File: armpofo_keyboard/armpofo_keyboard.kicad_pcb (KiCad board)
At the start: 2 copper layers, 180 x 76 mm, 94 parts, among them J1 Conn_01x16, M1 2,5mm, M10 2,5mm, M11 2,5mm, M12 2,5mm, M13 2,5mm, M14 2,5mm, M15 2,5mm, M16 2,5mm, M17 2,5mm, M18 2,5mm, M2 2,5mm, M3 2,5mm, M4 2,5mm, M5 2,5mm, M6 2,5mm, M7 2,5mm, M8 2,5mm, M9 2,5mm, SW1 Backspace, SW10 4, SW11 3, SW12 2, SW13 1, SW14 ESC, SW15 ], SW16 [, SW17 P, SW18 O, SW19 I, SW2 =+, SW20 U, SW21 Y, SW22 T, SW23 R, SW24 E, SW25 W, SW26 Q, SW27 TAB, SW28 ENTER, SW29 CAPS, SW3 -_, SW30 ' ", SW31 ;:, SW32 L, SW33 K, SW34 J, SW35 H, SW36 G, SW37 F, SW38 D, SW39 S, SW4 0, SW40 A, SW41 RSH, SW42 INS DEL, SW43 /?, SW44 .>, SW45 ,<, SW46 M, SW47 N, SW48 B, SW49 V, SW5 9, SW50 C, SW51 X, SW52 Z, SW53 \|, SW54 LSH, SW55 RIGHT, SW56 DOWN, SW57 UP, SW58 LEFT, SW59 SPACE, SW6 8, SW60 SPACE, SW61 ALT, SW62 CTRL, SW63 ATARI, SW64 FN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

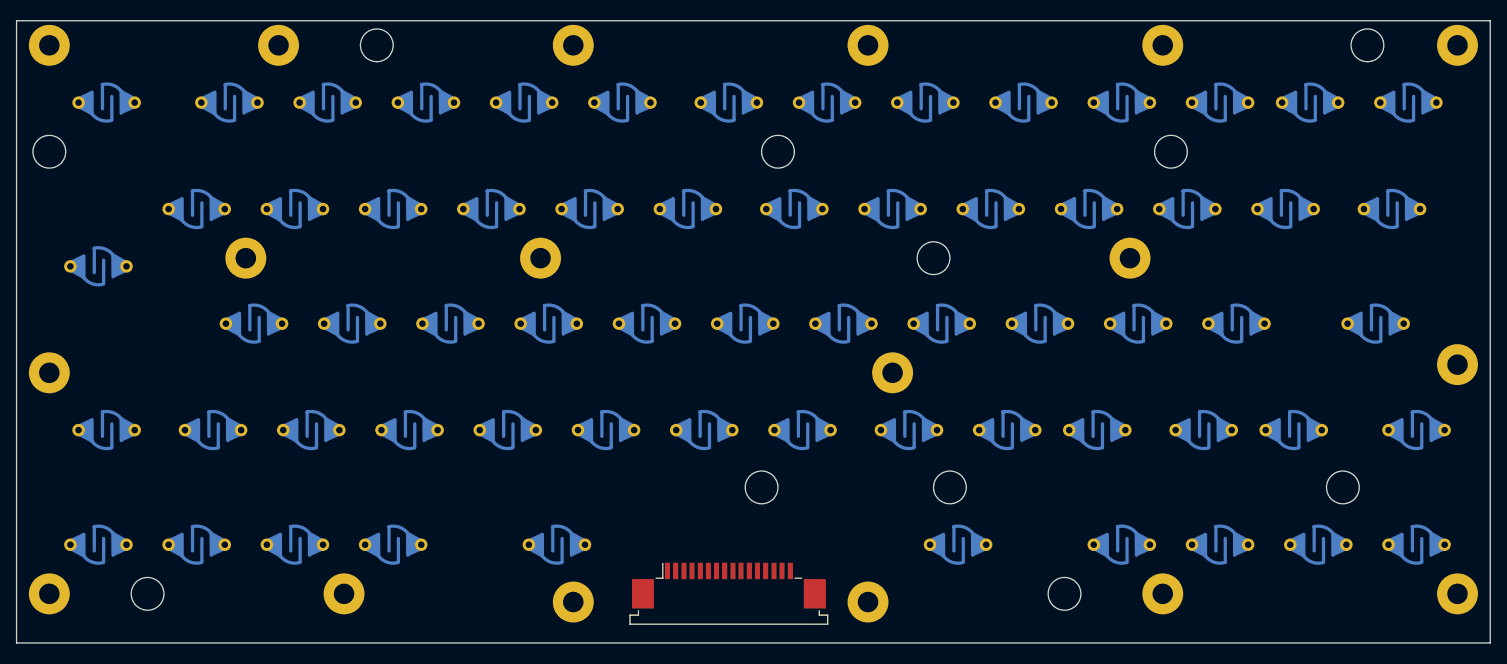
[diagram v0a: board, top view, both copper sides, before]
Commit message: holes are arranged to their final place
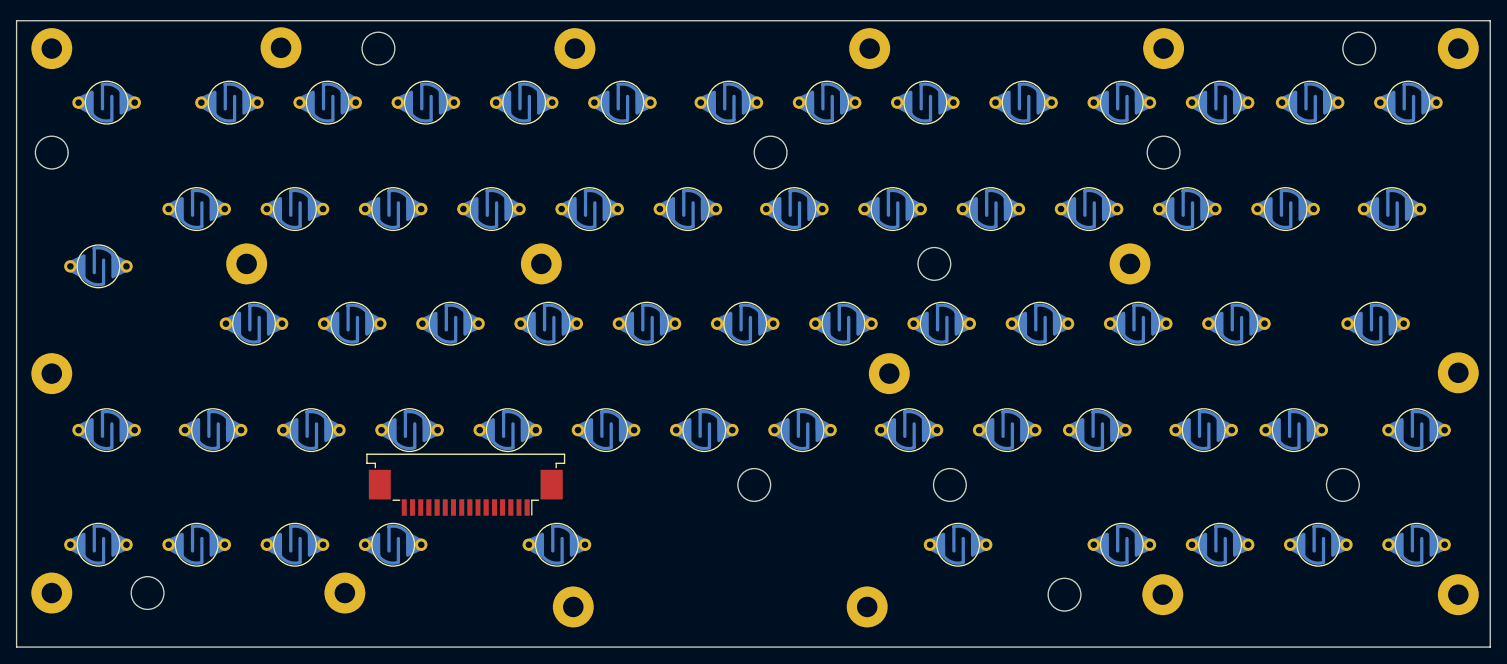
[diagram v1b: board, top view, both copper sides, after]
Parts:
- moved J1 34.1 mm to (54.9, -52.3), turned to 180 degrees
- moved H2 1.08 mm to (164.0, -106.6)
- moved M12 1.00 mm to (176.1, -67.0)
- moved H7 0.95 mm to (90.1, -53.3)
- moved H4 0.91 mm to (92.1, -93.9)
- moved H5 0.91 mm to (140.1, -93.9)
- moved M7 0.71 mm to (28.1, -80.3)
- moved H6 0.71 mm to (112.1, -80.3)
- moved M8 0.71 mm to (64.1, -80.3)
- moved M9 0.70 mm to (136.0, -80.3)
- moved M18 0.61 mm to (103.9, -38.4)
- moved M17 0.60 mm to (68.0, -38.4)
- moved M6 0.50 mm to (4.30, -106.6)
- moved H1 0.45 mm to (44.2, -106.6)
- moved M2 0.45 mm to (68.2, -106.6)
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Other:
- board size 180 x 76 mm -> 180 x 76.5 mm

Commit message: key landing at the final positions
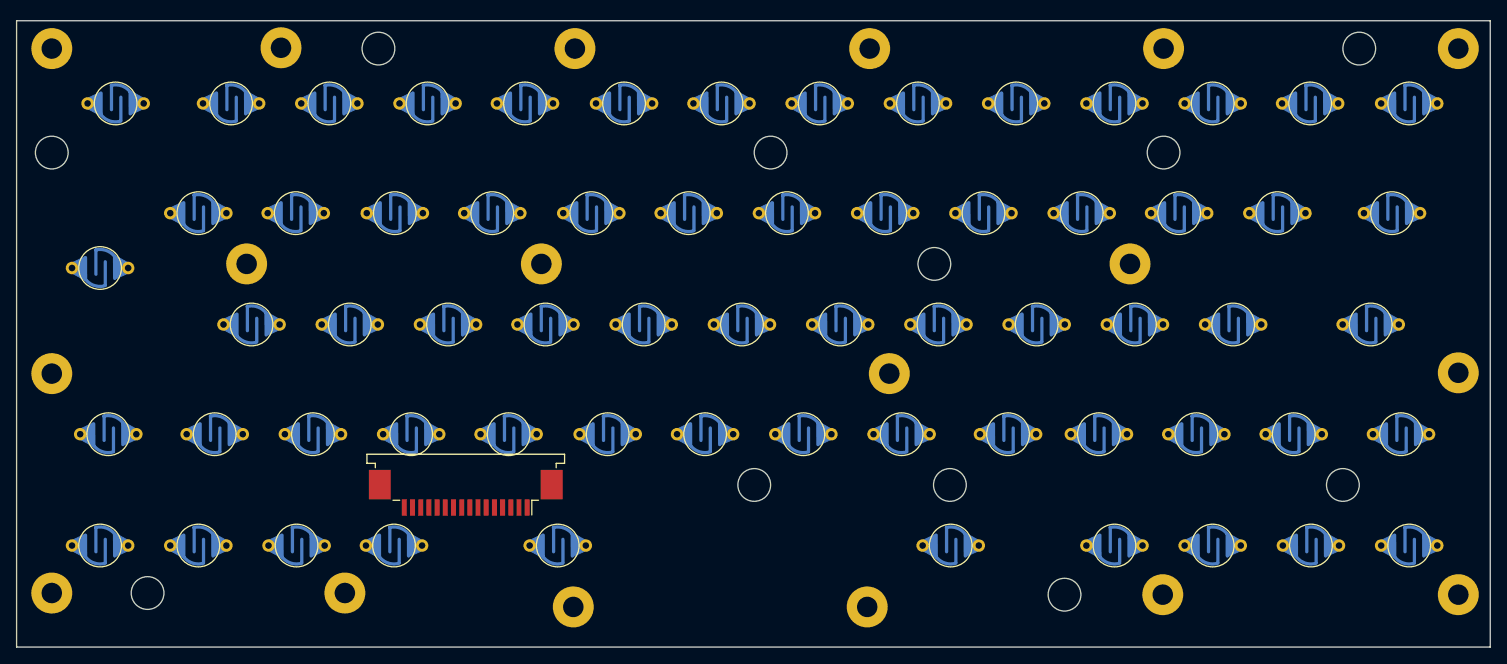
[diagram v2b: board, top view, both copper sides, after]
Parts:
- moved SW54 1.96 mm to (169.1, -59.5)
- moved SW25 1.12 mm to (142.0, -86.5)
- moved SW26 1.12 mm to (154.0, -86.5)
- moved SW1 1.10 mm to (12.1, -99.9)
- moved SW21 1.03 mm to (94.1, -86.5)
- moved SW22 1.03 mm to (106.1, -86.5)
- moved SW23 1.03 mm to (118.1, -86.5)
- moved SW24 1.03 mm to (130.1, -86.5)
- moved SW49 1.03 mm to (108.1, -59.5)
- moved SW52 1.03 mm to (144.1, -59.5)
- moved SW60 0.91 mm to (114.1, -45.9)
- moved SW61 0.91 mm to (134.1, -45.9)
- moved SW62 0.91 mm to (146.1, -45.9)
- moved SW63 0.91 mm to (158.1, -45.9)
- moved SW64 0.91 mm to (170.1, -45.9)
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
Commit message: small align adjustments
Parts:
- moved SW50 1.00 mm to (120.1, -59.5)
- moved H11 0.20 mm to (128.0, -39.7)
- moved H3 0.14 mm to (4.20, -93.8)
- moved H10 0.14 mm to (16.1, -40.0)
- moved M16 0.14 mm to (40.0, -40.0)
- moved M13 0.14 mm to (4.20, -40.0)
- moved M1 0.10 mm to (32.3, -106.6)
- moved M10 0.10 mm to (4.20, -66.9)
- moved M6 0.10 mm to (4.20, -106.6)
- moved M15 0.10 mm to (176.0, -39.9)
- moved M17 0.10 mm to (68.1, -38.4)
- moved M5 0.10 mm to (176.0, -106.6)
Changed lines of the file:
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@@
   )
   (module PROJECT_LOCAL:Key_landing (layer B.Cu)
-    (at 121.1 -59.5)
+    (at 120.1 -59.5)
     (fp_text reference SW50 (at -0.127 -3.556) (layer B.SilkS) hide
       (effects (font (size 1 1) (thickness 0.15)) (justify mirror))
@@
   )
   (module MountingHole:MountingHole_4mm (layer F.Cu)
-    (at 4.3 -93.9)
+    (at 4.2 -93.8)
     (descr "Mounting Hole 4mm, no annular")
     (tags "mounting hole 4mm no annular")
@@
   )
   (module MountingHole:MountingHole_4mm (layer F.Cu)
-    (at 16 -40.1)
+    (at 16.1 -40)
     (descr "Mounting Hole 4mm, no annular")
     (tags "mounting hole 4mm no annular")
@@
   )
   (module MountingHole:MountingHole_4mm (layer F.Cu)
-    (at 128 -39.9)
+    (at 128 -39.7)
     (descr "Mounting Hole 4mm, no annular")
     (tags "mounting hole 4mm no annular")
@@
   )
   (module MountingHole:MountingHole_2.5mm_Pad (layer F.Cu)
-    (at 32.3 -106.7)
+    (at 32.3 -106.6)
     (descr "Mounting Hole 2.5mm")
     (tags "mounting hole 2.5mm")
@@
   )
   (module MountingHole:MountingHole_2.5mm_Pad (layer F.Cu)
-    (at 176.1 -106.6)
+    (at 176 -106.6)
     (descr "Mounting Hole 2.5mm")
     (tags "mounting hole 2.5mm")
@@
   )
   (module MountingHole:MountingHole_2.5mm_Pad (layer F.Cu)
-    (at 4.3 -106.6)
+    (at 4.2 -106.6)
     (descr "Mounting Hole 2.5mm")
     (tags "mounting hole 2.5mm")
@@
   )
   (module MountingHole:MountingHole_2.5mm_Pad (layer F.Cu)
-    (at 4.3 -66.9)
+    (at 4.2 -66.9)
     (descr "Mounting Hole 2.5mm")
     (tags "mounting hole 2.5mm")
@@
   )
   (module MountingHole:MountingHole_2.5mm_Pad (layer F.Cu)
-    (at 4.3 -40.1)
+    (at 4.2 -40)
     (descr "Mounting Hole 2.5mm")
     (tags "mounting hole 2.5mm")
@@
   )
   (module MountingHole:MountingHole_2.5mm_Pad (layer F.Cu)
-    (at 176.1 -39.9)
+    (at 176 -39.9)
     (descr "Mounting Hole 2.5mm")
     (tags "mounting hole 2.5mm")
@@
   )
   (module MountingHole:MountingHole_2.5mm_Pad (layer F.Cu)
-    (at 40.1 -40.1)
+    (at 40 -40)
     (descr "Mounting Hole 2.5mm")
     (tags "mounting hole 2.5mm")
@@
   )
   (module MountingHole:MountingHole_2.5mm_Pad (layer F.Cu)
-    (at 68 -38.4)
-    (descr "Mounting Hole 2.5mm")
-    (tags "mounting hole 2.5mm")
+    (at 68.1 -38.4)
+    (descr "Mounting Hole 2.5mm")
+    (tags "mounting hole 2.5mm")

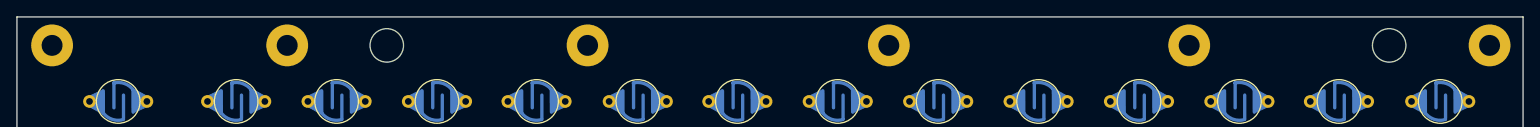
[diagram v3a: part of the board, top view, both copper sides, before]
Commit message: edge cut correction
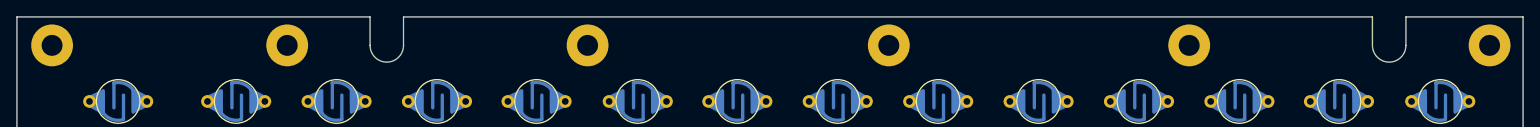
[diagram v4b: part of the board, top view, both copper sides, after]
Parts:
- removed H1, H2: 4mm, MountingHole:MountingHole_4mm
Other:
- outline, holes or cut-outs redrawn
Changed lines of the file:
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@@
   (general
     (thickness 1.6)
-    (drawings 4)
+    (drawings 12)
     (tracks 0)
     (zones 0)
-    (modules 94)
+    (modules 92)
     (nets 17)
   )
@@
   )
   (module MountingHole:MountingHole_4mm (layer F.Cu)
-    (at 44.2 -106.6)
-    (descr "Mounting Hole 4mm, no annular")
-    (tags "mounting hole 4mm no annular")
-    (attr virtual)
-    (fp_text reference H1 (at 0 -5) (layer F.SilkS) hide
-      (effects (font (size 1 1) (thickness 0.15)))
-    )
-    (fp_text value 4mm (at 0 5) (layer F.Fab)
-      (effects (font (size 1 1) (thickness 0.15)))
-    )
-    (fp_circle (center 0 0) (end 4 0) (layer Cmts.User) (width 0.15))
-    (fp_circle (center 0 0) (end 4.25 0) (layer F.CrtYd) (width 0.05))
-    (fp_text user %R (at 0.3 0) (layer F.Fab) hide
-      (effects (font (size 1 1) (thickness 0.15)))
-    )
-    (pad 1 np_thru_hole circle (at 0 0) (size 4 4) (drill 4) (layers *.Cu *.Mask))
-  )
-  (module MountingHole:MountingHole_4mm (layer F.Cu)
-    (at 164 -106.6)
-    (descr "Mounting Hole 4mm, no annular")
-    (tags "mounting hole 4mm no annular")
-    (attr virtual)
-    (fp_text reference H2 (at 0 -5) (layer F.SilkS) hide
-      (effects (font (size 1 1) (thickness 0.15)))
-    )
-    (fp_text value 4mm (at 0 5) (layer F.Fab)
-      (effects (font (size 1 1) (thickness 0.15)))
-    )
-    (fp_circle (center 0 0) (end 4 0) (layer Cmts.User) (width 0.15))
-    (fp_circle (center 0 0) (end 4.25 0) (layer F.CrtYd) (width 0.05))
-    (fp_text user %R (at 0.3 0) (layer F.Fab) hide
-      (effects (font (size 1 1) (thickness 0.15)))
-    )
-    (pad 1 np_thru_hole circle (at 0 0) (size 4 4) (drill 4) (layers *.Cu *.Mask))
-  )
-  (module MountingHole:MountingHole_4mm (layer F.Cu)
     (at 4.2 -93.8)
     (descr "Mounting Hole 4mm, no annular")
@@
     )
   )
+  (gr_line (start 166 -110) (end 180 -110) (layer Edge.Cuts) (width 0.05))
+  (gr_line (start 46.2 -110) (end 162 -110) (layer Edge.Cuts) (width 0.05))
+  (gr_line (start 46.2 -106.6) (end 46.2 -110) (layer Edge.Cuts) (width 0.05))
+  (gr_line (start 42.2 -106.6) (end 42.2 -110) (layer Edge.Cuts) (width 0.05))
+  (gr_line (start 166 -106.6) (end 166 -110) (layer Edge.Cuts) (width 0.05))
+  (gr_line (start 162 -106.6) (end 162 -110) (layer Edge.Cuts) (width 0.05))
+  (gr_arc (start 164 -106.6) (end 162 -106.6) (angle -180) (layer Edge.Cuts) (width 0.05))
+  (gr_arc (start 44.2 -106.6) (end 42.2 -106.6) (angle -180) (layer Edge.Cuts) (width 0.05))
   (gr_line (start 0 -33.5) (end 0 -110) (layer Edge.Cuts) (width 0.05))
   (gr_line (start 180 -33.5) (end 0 -33.5) (layer Edge.Cuts) (width 0.05))
   (gr_line (start 180 -110) (end 180 -33.5) (layer Edge.Cuts) (width 0.05))
-  (gr_line (start 0 -110) (end 180 -110) (layer Edge.Cuts) (width 0.05))
+  (gr_line (start 0 -110) (end 42.2 -110) (layer Edge.Cuts) (width 0.05))
 )

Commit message: routing finished
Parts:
- moved J1 1.00 mm to (55.8, -52.0)
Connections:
- M1 pad 1: (no net) -> GND
- M10 pad 1: (no net) -> GND
- M11 pad 1: (no net) -> GND
- M12 pad 1: (no net) -> GND
- M13 pad 1: (no net) -> GND
- M14 pad 1: (no net) -> GND
- M15 pad 1: (no net) -> GND
- M16 pad 1: (no net) -> GND
- M17 pad 1: (no net) -> GND
- M18 pad 1: (no net) -> GND
- M2 pad 1: (no net) -> GND
- M3 pad 1: (no net) -> GND
- M4 pad 1: (no net) -> GND
- M5 pad 1: (no net) -> GND
- M6 pad 1: (no net) -> GND
- M7 pad 1: (no net) -> GND
- M8 pad 1: (no net) -> GND
- M9 pad 1: (no net) -> GND
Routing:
- net /R6: track 0.00 -> 338.9 mm, vias 0 -> 3
- net /R3: track 0.00 -> 325.6 mm, vias 0 -> 4
- net /C4: track 0.00 -> 306.9 mm, vias 0 -> 1
- net /R1: track 0.00 -> 301.6 mm, vias 0 -> 4
- net /C2: track 0.00 -> 299.8 mm, vias 0 -> 2
- net /R8: track 0.00 -> 296.2 mm, vias 0 -> 3
- net /R7: track 0.00 -> 295.4 mm, vias 0 -> 3
- net /R5: track 0.00 -> 273.9 mm, vias 0 -> 4
- net /R4: track 0.00 -> 273.0 mm, vias 0 -> 4
- net /C3: track 0.00 -> 268.0 mm, vias 0 -> 2
- net /C1: track 0.00 -> 265.7 mm, vias 0 -> 1
- net /C5: track 0.00 -> 241.7 mm, vias 0 -> 4
- net /C6: track 0.00 -> 229.6 mm, vias 0 -> 1
- net /C7: track 0.00 -> 217.0 mm, vias 0 -> 2
- net /C8: track 0.00 -> 209.1 mm, vias 0 -> 4
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- added copper zone on F.Cu, net GND

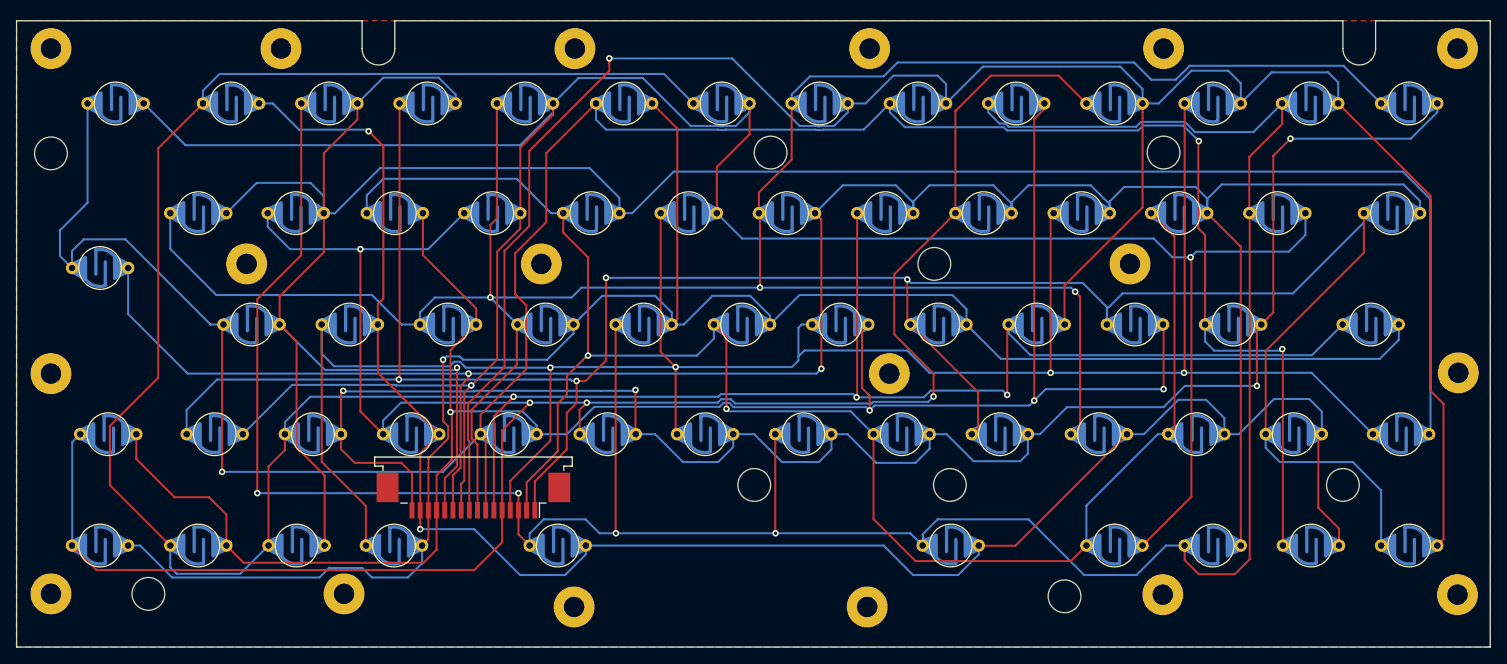
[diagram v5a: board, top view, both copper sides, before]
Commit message: - CPU board finalisch edge cuts - Keyboard mounting modified to 2.2 mm holes
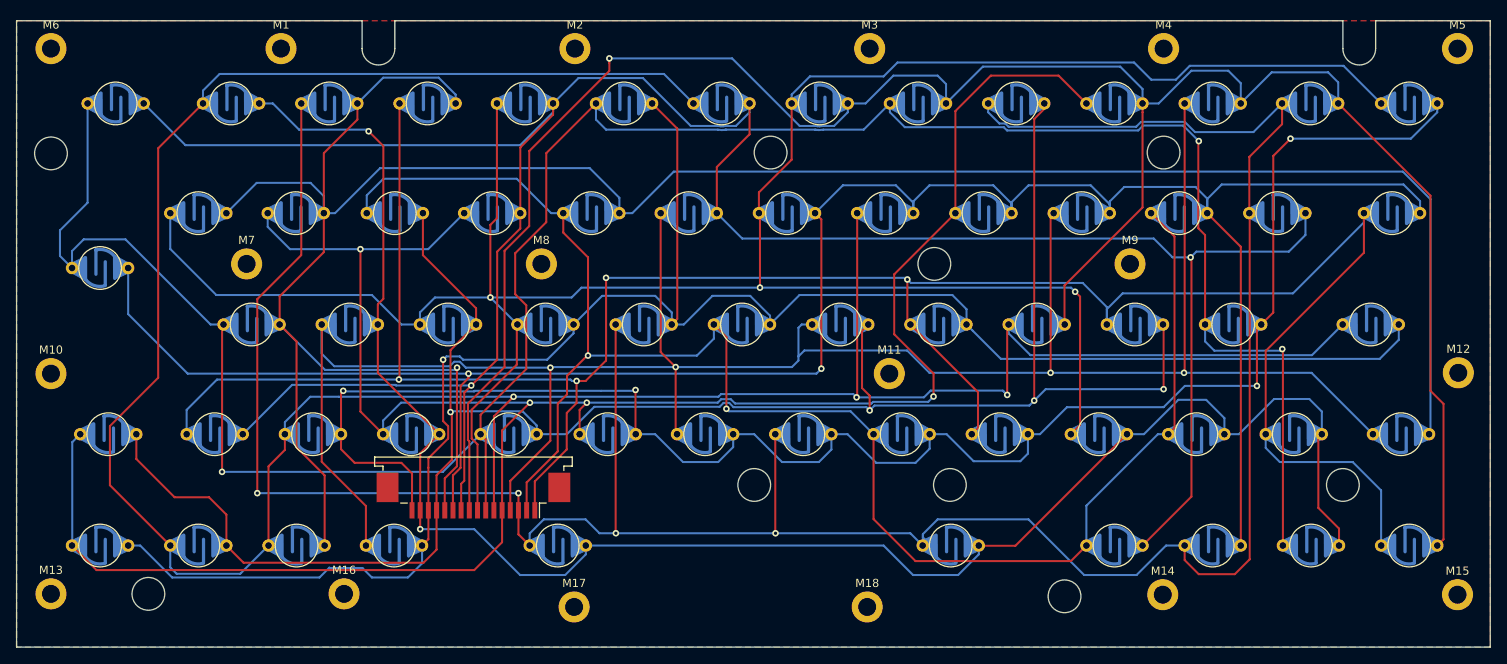
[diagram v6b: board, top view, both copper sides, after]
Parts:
- M1, M10, M11, M12, M13, M14, M15, M16, M17, M18, M2, M3, M4, M5, M6, M7, M8, M9: value 2,5mm -> 2,1mm; footprint MountingHole:MountingHole_2.5mm_Pad -> MountingHole:MountingHole_2.2mm_M2_DIN965_Pad

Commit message: gerber files generated
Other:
- board text added: "ARMPOFO KEYBOARD"
- board text added: "C8"
- board text added: "R1"
